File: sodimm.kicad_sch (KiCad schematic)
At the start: 0 parts

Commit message: [#100470] Add SODIMM connector to schematic
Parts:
- added J1: PCB-Edge_SODIMM_144, symbol antmicroEdgeConnectors:PCB-Edge_SODIMM_144
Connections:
- new net +3.3V: J1.101 (Vdd), J1.102 (A6), J1.11 (Vdd), J1.113 (Vdd), J1.114 (Vdd), J1.12 (Vdd), J1.129 (Vdd), J1.130 (Vdd), J1.143 (Vdd), J1.144 (Vdd), J1.27 (Vdd), J1.28 (Vdd), J1.45 (Vdd), J1.46 (Vdd), J1.63 (Vdd), J1.64 (Vdd), J1.81 (Vdd), J1.82 (Vdd)
- new net A0: J1.29 (A0)
- new net A1: J1.31 (A1)
- new net A10: J1.111 (A10/AP)
- new net A11: J1.112 (A11)
- new net A12: J1.70 (A12)
- new net A2: J1.33 (A2)
- new net A3: J1.30 (A3)
- new net A4: J1.32 (A4)
- new net A5: J1.34 (A5)
- new net A6: J1.102 (A6)
- new net A7: J1.104 (A7)
- new net A8: J1.105 (A8)
- new net A9: J1.109 (A9)
- new net BA0: J1.106 (BA0)
- new net BA1: J1.110 (BA1)
- new net CAS: J1.66 (CAS)
- new net DQ0: J1.3 (DQ0)
- new net DQ1: J1.5 (DQ1)
- new net DQ10: J1.41 (DQ10)
- new net DQ11: J1.43 (DQ11)
- new net DQ12: J1.47 (DQ12)
- new net DQ13: J1.49 (DQ13)
- new net DQ14: J1.51 (DQ14)
- new net DQ15: J1.53 (DQ15)
- new net DQ16: J1.83 (DQ16)
- new net DQ17: J1.85 (DQ17)
- new net DQ18: J1.87 (DQ18)
- new net DQ19: J1.89 (DQ19)
- new net DQ2: J1.7 (DQ2)
- new net DQ20: J1.93 (DQ20)
- new net DQ21: J1.95 (DQ21)
- new net DQ22: J1.97 (DQ22)
- new net DQ23: J1.99 (DQ23)
- new net DQ24: J1.121 (DQ24)
- new net DQ25: J1.123 (DQ25)
- new net DQ26: J1.125 (DQ26)
- new net DQ27: J1.127 (DQ27)
- new net DQ28: J1.131 (DQ28)
- new net DQ29: J1.133 (DQ29)
- new net DQ3: J1.9 (DQ3)
- new net DQ30: J1.135 (DQ30)
- new net DQ31: J1.137 (DQ31)
- new net DQ4: J1.13 (DQ4)
- new net DQ5: J1.15 (DQ5)
- new net DQ6: J1.17 (DQ6)
- new net DQ7: J1.19 (DQ7)
- new net DQ8: J1.37 (DQ8)
- new net DQ9: J1.39 (DQ9)
- new net DQMB0: J1.23 (DQMB0)
- new net DQMB1: J1.25 (DQMB1)
- new net DQMB2: J1.115 (DQMB2)
- new net DQMB3: J1.117 (DQMB3)
- new net GND: J1.1 (Vss), J1.107 (Vss), J1.108 (Vss), J1.119 (Vss), J1.120 (Vss), J1.139 (Vss), J1.140 (Vss), J1.2 (Vss), J1.21 (Vss), J1.22 (Vss), J1.35 (Vss), J1.36 (Vss), J1.55 (Vss), J1.56 (Vss), J1.75 (Vss), J1.76 (Vss), J1.91 (Vss), J1.92 (Vss)
- new net RAS: J1.65 (RAS)
- new net S0: J1.69 (S0)
- new net S1: J1.71 (S1)
- new net WE: J1.67 (WE)
- no-connect marks 0 -> 43

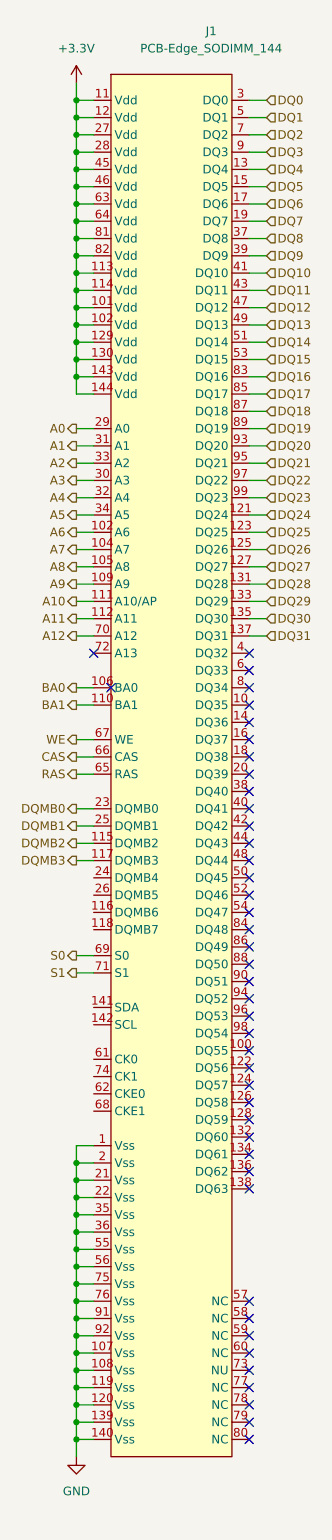
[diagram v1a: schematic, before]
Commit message: [#100470] Connect SODIMM to SDRAM banks
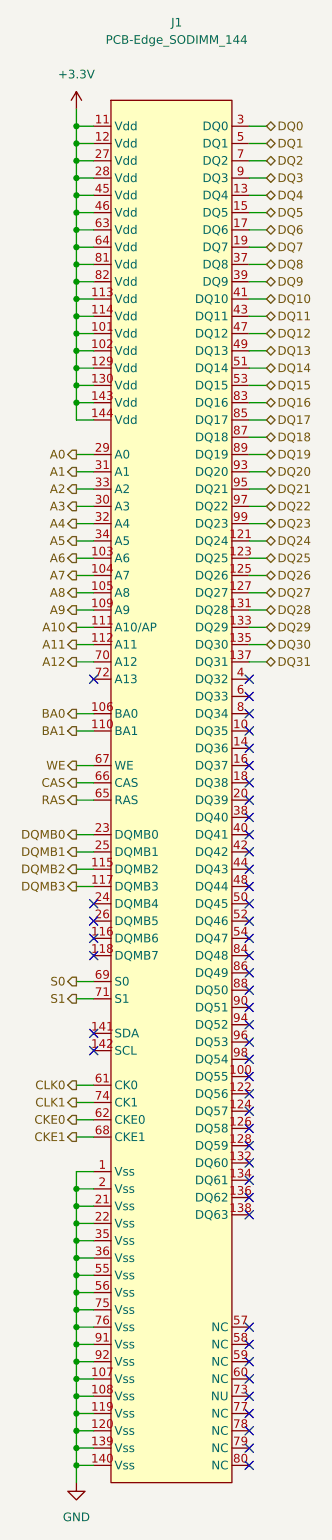
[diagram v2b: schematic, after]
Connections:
- net A6: now also J1.103 (A6); no longer J1.102 (A6)
- net CLK0: now reaches J1.61 (CK0)
- net CKE0: now reaches J1.62 (CKE0)
- net CKE1: now reaches J1.68 (CKE1)
- net CLK1: now reaches J1.74 (CK1)
- no-connect marks 43 -> 48
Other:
- company: (none) -> Antmicro Ltd
- title: (none) -> STM32H7 HDMI Board SODIMM
- moved on the sheet: J1

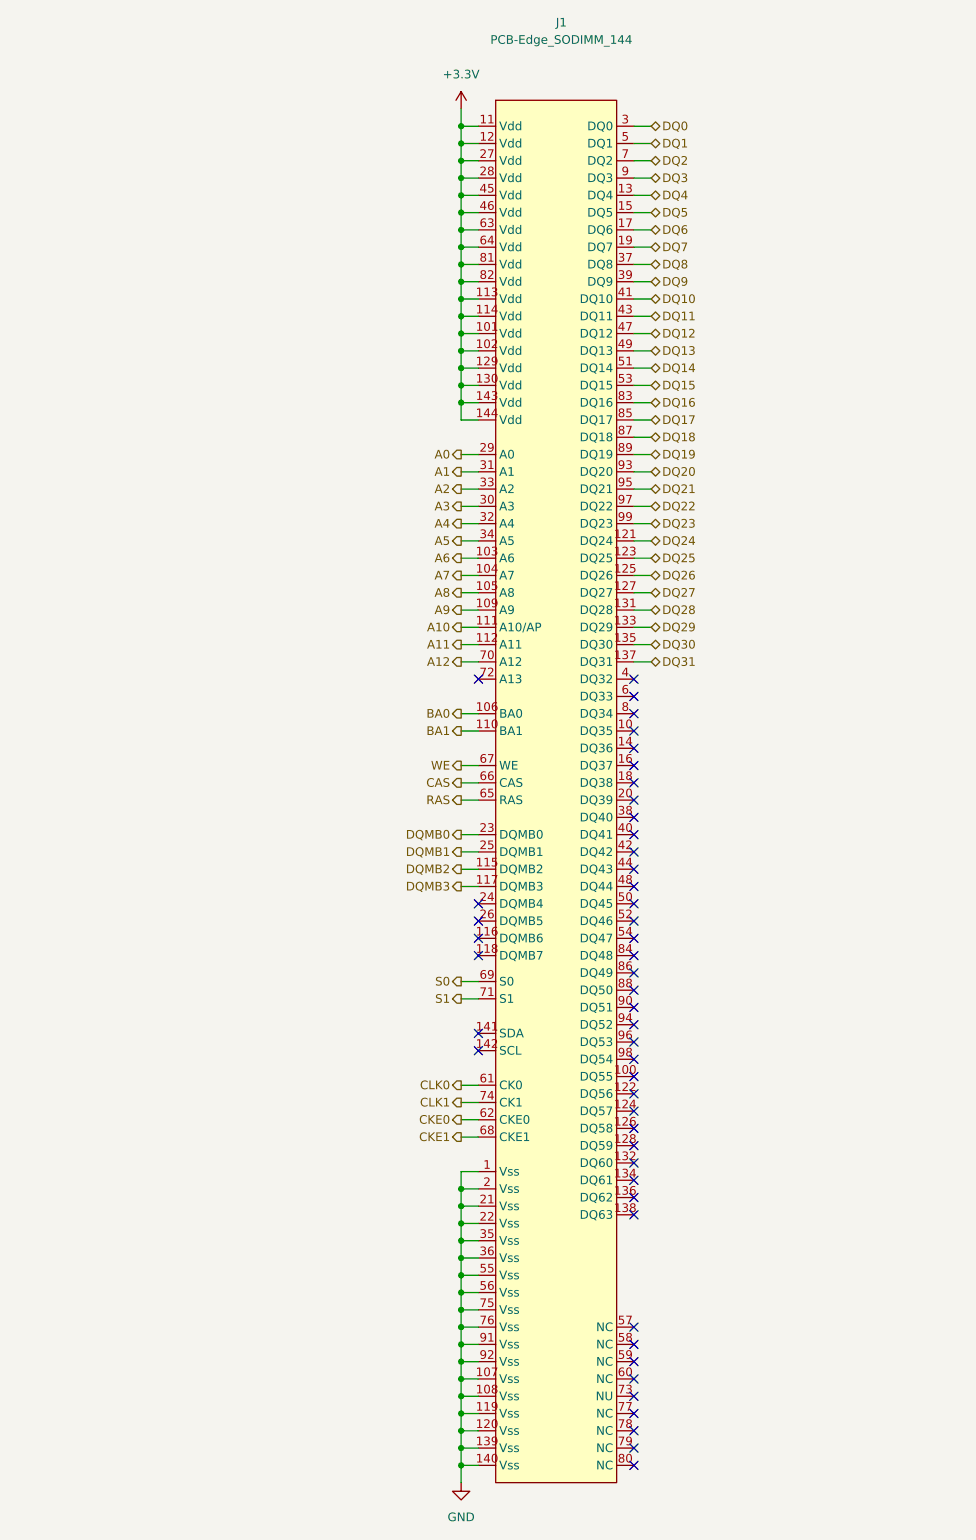
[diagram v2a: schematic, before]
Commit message: [#100470] Update SODIMM 144 pin connector
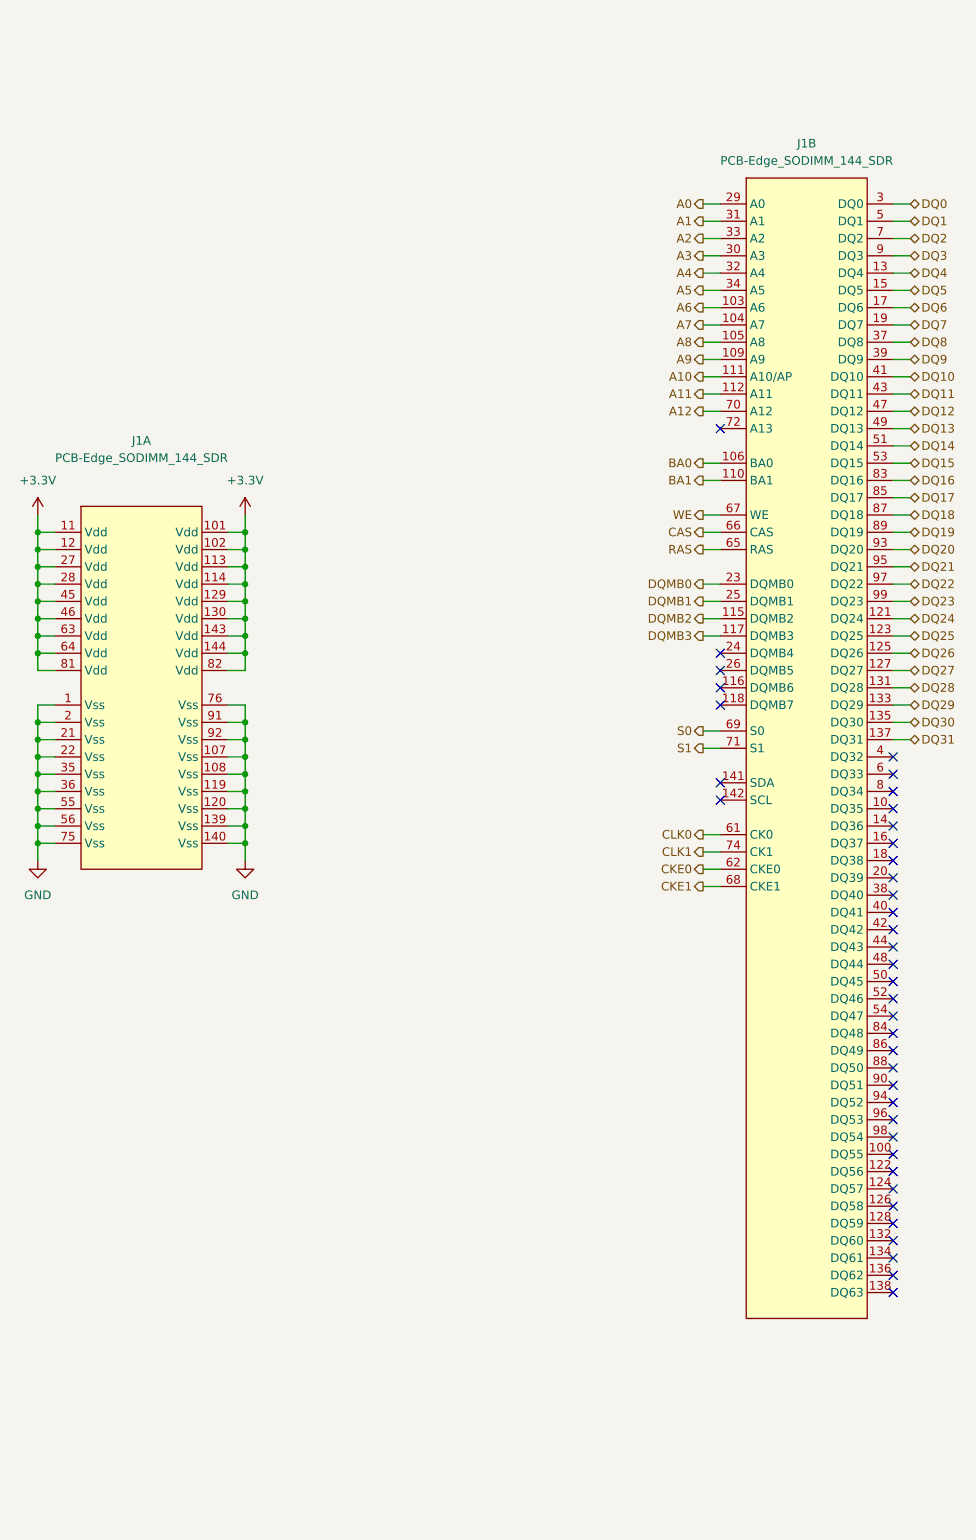
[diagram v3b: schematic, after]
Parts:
- removed J1: PCB-Edge_SODIMM_144, symbol antmicroEdgeConnectors:PCB-Edge_SODIMM_144
- added J1: PCB-Edge_SODIMM_144_SDR, antmicro-footprints:PCB-Edge_SODIMM_144_SDR, symbol antmicroEdgeConnectors:PCB-Edge_SODIMM_144_SDR
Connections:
- net +3.3V: now also J1.101 (Vdd), J1.102 (Vdd), J1.11 (Vdd), J1.113 (Vdd), J1.114 (Vdd), J1.12 (Vdd), J1.129 (Vdd), J1.130 (Vdd), J1.143 (Vdd), J1.144 (Vdd), J1.27 (Vdd), J1.28 (Vdd), J1.45 (Vdd), J1.46 (Vdd), J1.63 (Vdd), J1.64 (Vdd), J1.81 (Vdd), J1.82 (Vdd)
- net A0: now also J1.29 (A0)
- net A1: now also J1.31 (A1)
- net A10: now also J1.111 (A10/AP)
- net A11: now also J1.112 (A11)
- net A12: now also J1.70 (A12)
- net A2: now also J1.33 (A2)
- net A3: now also J1.30 (A3)
- net A4: now also J1.32 (A4)
- net A5: now also J1.34 (A5)
- net A6: now also J1.103 (A6)
- net A7: now also J1.104 (A7)
- net A8: now also J1.105 (A8)
- net A9: now also J1.109 (A9)
- net BA0: now also J1.106 (BA0)
- net BA1: now also J1.110 (BA1)
- net CAS: now also J1.66 (CAS)
- net CKE0: now also J1.62 (CKE0)
- net CKE1: now also J1.68 (CKE1)
- net CLK0: now also J1.61 (CK0)
- net CLK1: now also J1.74 (CK1)
- net DQ0: now also J1.3 (DQ0)
- net DQ1: now also J1.5 (DQ1)
- net DQ10: now also J1.41 (DQ10)
- net DQ11: now also J1.43 (DQ11)
- net DQ12: now also J1.47 (DQ12)
- net DQ13: now also J1.49 (DQ13)
- net DQ14: now also J1.51 (DQ14)
- net DQ15: now also J1.53 (DQ15)
- net DQ16: now also J1.83 (DQ16)
- net DQ17: now also J1.85 (DQ17)
- net DQ18: now also J1.87 (DQ18)
- net DQ19: now also J1.89 (DQ19)
- net DQ2: now also J1.7 (DQ2)
- net DQ20: now also J1.93 (DQ20)
- net DQ21: now also J1.95 (DQ21)
- net DQ22: now also J1.97 (DQ22)
- net DQ23: now also J1.99 (DQ23)
- net DQ24: now also J1.121 (DQ24)
- net DQ25: now also J1.123 (DQ25)
- net DQ26: now also J1.125 (DQ26)
- net DQ27: now also J1.127 (DQ27)
- net DQ28: now also J1.131 (DQ28)
- net DQ29: now also J1.133 (DQ29)
- net DQ3: now also J1.9 (DQ3)
- net DQ30: now also J1.135 (DQ30)
- net DQ31: now also J1.137 (DQ31)
- net DQ4: now also J1.13 (DQ4)
- net DQ5: now also J1.15 (DQ5)
- net DQ6: now also J1.17 (DQ6)
- net DQ7: now also J1.19 (DQ7)
- net DQ8: now also J1.37 (DQ8)
- net DQ9: now also J1.39 (DQ9)
- net DQMB0: now also J1.23 (DQMB0)
- net DQMB1: now also J1.25 (DQMB1)
- net DQMB2: now also J1.115 (DQMB2)
- net DQMB3: now also J1.117 (DQMB3)
- net GND: now also J1.1 (Vss), J1.107 (Vss), J1.108 (Vss), J1.119 (Vss), J1.120 (Vss), J1.139 (Vss), J1.140 (Vss), J1.2 (Vss), J1.21 (Vss), J1.22 (Vss), J1.35 (Vss), J1.36 (Vss), J1.55 (Vss), J1.56 (Vss), J1.75 (Vss), J1.76 (Vss), J1.91 (Vss), J1.92 (Vss)
- net RAS: now also J1.65 (RAS)
- net S0: now also J1.69 (S0)
- net S1: now also J1.71 (S1)
- net WE: now also J1.67 (WE)
- new net: J1.57 (NC), J1.58 (NC), J1.59 (NC), J1.60 (NC), J1.73 (NU), J1.77 (NC), J1.78 (NC), J1.79 (NC), J1.80 (NC)
- no-connect marks 48 -> 39

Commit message: [#100470] Add 1u decoupling capacitors to schematic
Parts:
- J1: Author (none) -> Antmicro; License (none) -> Apache-2.0

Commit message: [#100470] Update schematic
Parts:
- removed unit 2 of J1
- added unit 3 of J1
- added unit 4 of J1
- added J2: PCB-Edge_SODIMM_144_SDR, antmicro-footprints:PCB-Edge_SODIMM_144_SDR, symbol antmicroEdgeConnectors:PCB-Edge_SODIMM_144_SDR
- added TP1, TP2: TestPoint, symbol Connector:TestPoint
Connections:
- net A0: now also J2.29 (A0)
- net A1: now also J2.31 (A1)
- net A10: now also J2.111 (A10/AP)
- net A11: now also J2.112 (A11)
- net A12: now also J2.70 (A12)
- net A2: now also J2.33 (A2)
- net A3: now also J2.30 (A3)
- net A4: now also J2.32 (A4)
- net A5: now also J2.34 (A5)
- net A6: now also J2.103 (A6)
- net A7: now also J2.104 (A7)
- net A8: now also J2.105 (A8)
- net A9: now also J2.109 (A9)
- net BA0: now also J2.106 (BA0)
- net BA1: now also J2.110 (BA1)
- net CAS: now also J2.66 (CAS)
- net CKE0: now also J2.62 (CKE0)
- net CKE1: now also J2.68 (CKE1)
- net CLK0: now also J2.61 (CK0)
- net CLK1: now also J2.74 (CK1)
- net DQ0: now also J1.3 (DQ0)
- net DQ1: now also J1.5 (DQ1)
- net DQ10: now also J1.41 (DQ10)
- net DQ11: now also J1.43 (DQ11)
- net DQ12: now also J1.47 (DQ12)
- net DQ13: now also J1.49 (DQ13)
- net DQ14: now also J1.51 (DQ14)
- net DQ15: now also J1.53 (DQ15)
- net DQ16: now also J1.83 (DQ16)
- net DQ17: now also J1.85 (DQ17)
- net DQ18: now also J1.87 (DQ18)
- net DQ19: now also J1.89 (DQ19)
- net DQ2: now also J1.7 (DQ2)
- net DQ20: now also J1.93 (DQ20)
- net DQ21: now also J1.95 (DQ21)
- net DQ22: now also J1.97 (DQ22)
- net DQ23: now also J1.99 (DQ23)
- net DQ24: now also J1.121 (DQ24)
- net DQ25: now also J1.123 (DQ25)
- net DQ26: now also J1.125 (DQ26)
- net DQ27: now also J1.127 (DQ27)
- net DQ28: now also J1.131 (DQ28)
- net DQ29: now also J1.133 (DQ29)
- net DQ3: now also J1.9 (DQ3)
- net DQ30: now also J1.135 (DQ30)
- net DQ31: now also J1.137 (DQ31)
- net DQ4: now also J1.13 (DQ4)
- net DQ5: now also J1.15 (DQ5)
- net DQ6: now also J1.17 (DQ6)
- net DQ7: now also J1.19 (DQ7)
- net DQ8: now also J1.37 (DQ8)
- net DQ9: now also J1.39 (DQ9)
- net DQMB0: now also J1.23 (DQMB0)
- net DQMB1: now also J1.25 (DQMB1)
- net DQMB2: now also J1.115 (DQMB2)
- net DQMB3: now also J1.117 (DQMB3)
- net RAS: now also J2.65 (RAS)
- net S0: now also J2.69 (S0)
- net S1: now also J2.71 (S1)
- net WE: now also J2.67 (WE)
- new net: J2.141 (SDA), TP1.1
- new net: J2.142 (SCL), TP2.1
- new net: J2.57 (NC), J2.58 (NC), J2.59 (NC), J2.60 (NC), J2.73 (NU), J2.77 (NC), J2.78 (NC), J2.79 (NC), J2.80 (NC)
- no-connect marks 39 -> 37
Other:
- moved on the sheet: J1A

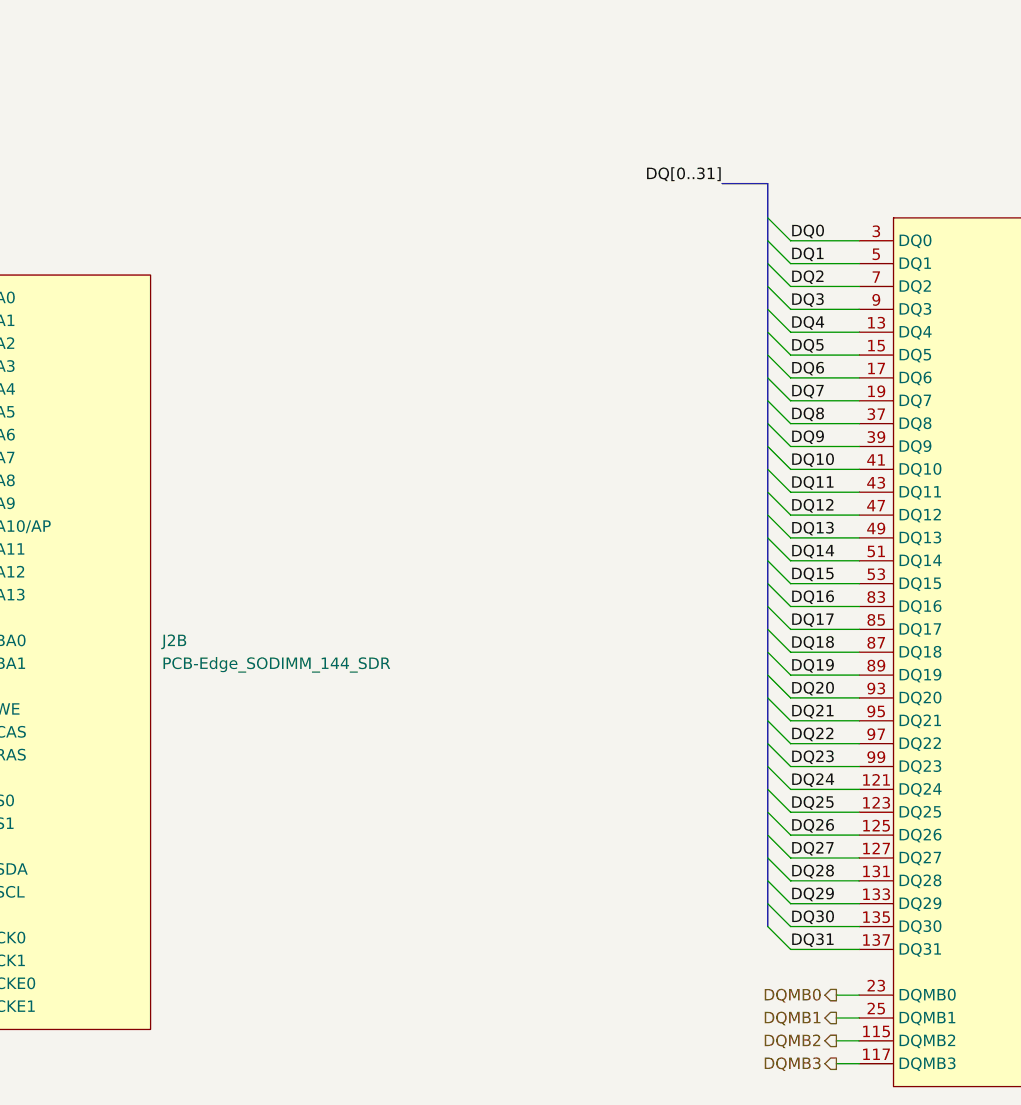
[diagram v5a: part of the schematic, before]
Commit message: [#100650] PCB layout update - placing ICs
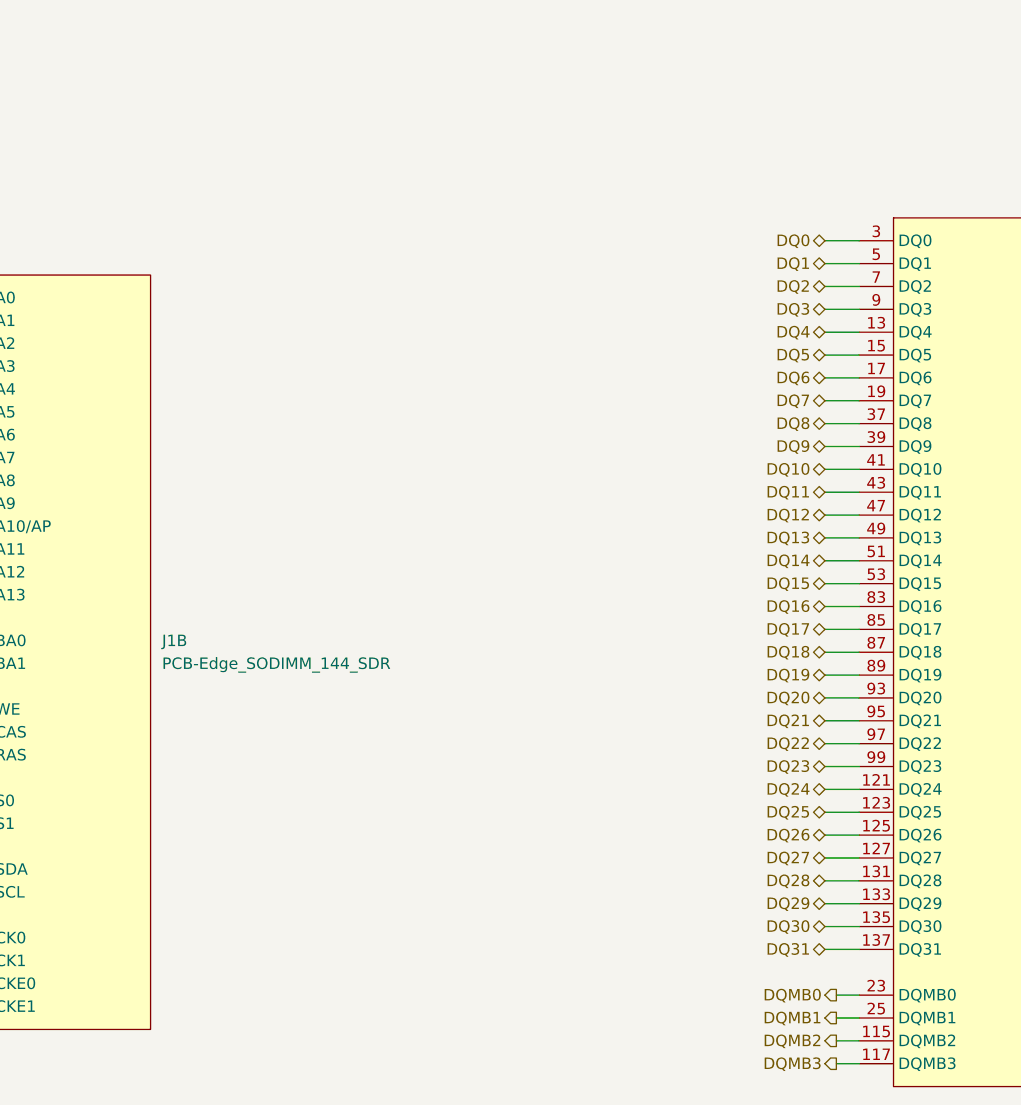
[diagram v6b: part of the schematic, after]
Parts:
- J1: now left out of the parts list
- renumbered J2 to J1
